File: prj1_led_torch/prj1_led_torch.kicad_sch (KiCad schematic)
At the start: 4 parts, among them SW1 SW_SPST

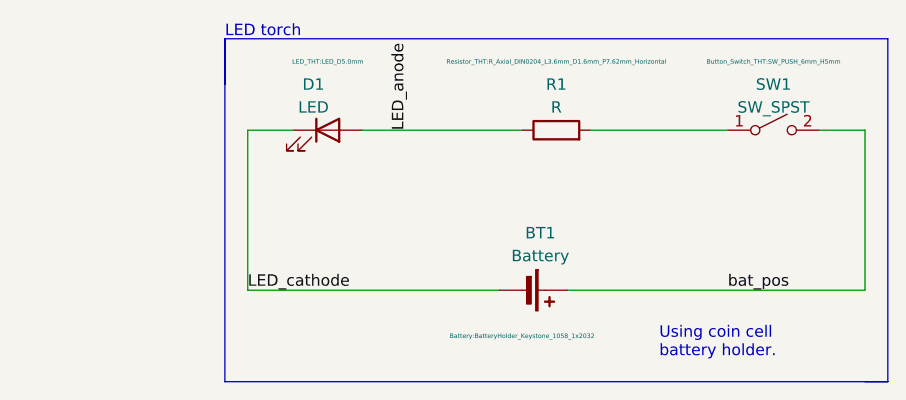
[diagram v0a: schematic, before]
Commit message: Creata simulazione circuitale
Feat: preparata la simulazione per transitorio
Feat: creato il modello per il diodo LED
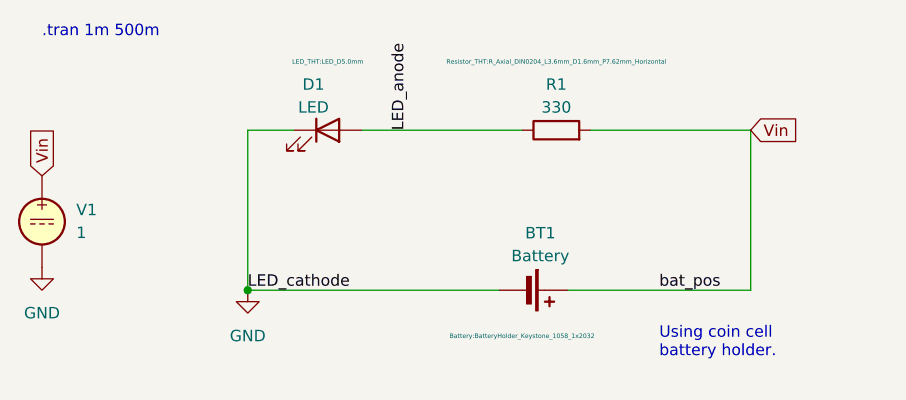
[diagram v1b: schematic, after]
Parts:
- removed SW1: SW_SPST, Button_Switch_THT:SW_PUSH_6mm_H5mm, symbol Switch:SW_SPST
- added V1: 1, symbol Simulation_SPICE:VDC
- R1: value R -> 330
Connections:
- net bat_pos is gone; now on net Vin: BT1.1 (+)
- net Vin: now reaches R1.2
- net Vin: now also V1.1
- net LED_cathode renamed GND
- net GND: now also V1.2
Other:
- note added: ".tran 1m 500m"
- note removed: "LED torch"
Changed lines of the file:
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@@
     (comment 2 "Filippo Graziani")
   )
+  (junction (at 116.84 109.22) (diameter 0) (color 0 0 0 0)
+  )
   (wire (pts (xy 129.54 91.44) (xy 147.32 91.44))
     (stroke (width 0) (type default))
   )
-  (polyline (pts (xy 114.3 81.28) (xy 114.3 86.36))
-    (stroke (width 0) (type default))
-  )
-  (wire (pts (xy 154.94 91.44) (xy 170.18 91.44))
-    (stroke (width 0) (type default))
-  )
-  (wire (pts (xy 185.42 91.44) (xy 185.42 109.22))
+  (wire (pts (xy 152.4 109.22) (xy 172.72 109.22))
+    (stroke (width 0) (type default))
+  )
+  (wire (pts (xy 172.72 91.44) (xy 172.72 109.22))
     (stroke (width 0) (type default))
   )
@@
     (stroke (width 0) (type default))
   )
-  (polyline (pts (xy 114.3 81.28) (xy 187.96 81.28))
-    (stroke (width 0) (type default))
-  )
-  (wire (pts (xy 152.4 109.22) (xy 185.42 109.22))
-    (stroke (width 0) (type default))
-  )
-  (polyline (pts (xy 187.96 119.38) (xy 114.3 119.38))
-    (stroke (width 0) (type default))
-  )
-  (polyline (pts (xy 114.3 81.28) (xy 114.3 119.38))
-    (stroke (width 0) (type default))
-  )
-  (wire (pts (xy 180.34 91.44) (xy 185.42 91.44))
-    (stroke (width 0) (type default))
-  )
-  (polyline (pts (xy 185.42 119.38) (xy 187.96 119.38))
-    (stroke (width 0) (type default))
-  )
-  (polyline (pts (xy 187.96 81.28) (xy 187.96 119.38))
+  (wire (pts (xy 154.94 91.44) (xy 172.72 91.44))
     (stroke (width 0) (type default))
   )
@@
     (effects (font (size 1.27 1.27)) (justify left bottom))
   )
-  (text "LED torch" (at 114.3 81.28 0)
+  (text ".tran 1m 500m" (at 93.98 81.28 0)
     (effects (font (size 1.27 1.27)) (justify left bottom))
   )
@@
     (effects (font (size 1.27 1.27)) (justify left bottom))
   )
-  (label "bat_pos" (at 170.18 109.22 0) (fields_autoplaced)
-    (effects (font (size 1.27 1.27)) (justify left bottom))
+  (label "bat_pos" (at 162.56 109.22 0) (fields_autoplaced)
+    (effects (font (size 1.27 1.27)) (justify left bottom))
+  )
+  (global_label "Vin" (shape input) (at 172.72 91.44 0) (fields_autoplaced)
+    (effects (font (size 1.27 1.27)) (justify left))
+    (property "Intersheetrefs" "${INTERSHEET_REFS}" (at 178.4682 91.44 0)
+      (effects (font (size 1.27 1.27)) (justify left) hide)
+    )
+  )
+  (global_label "Vin" (shape input) (at 93.98 96.52 90) (fields_autoplaced)
+    (effects (font (size 1.27 1.27)) (justify left))
+    (property "Intersheetrefs" "${INTERSHEET_REFS}" (at 93.98 90.7718 90)
+      (effects (font (size 1.27 1.27)) (justify left) hide)
+    )
+  )
+  (symbol (lib_id "power:GND") (at 93.98 106.68 0) (unit 1)
+    (in_bom yes) (on_board yes) (dnp no) (fields_autoplaced)
+    (property "Reference" "#PWR01" (at 93.98 113.03 0)
+      (effects (font (size 1.27 1.27)) hide)
+    )
+    (property "Value" "GND" (at 93.98 111.76 0)
+      (effects (font (size 1.27 1.27)))
+    )
+    (property "Footprint" "" (at 93.98 106.68 0)
+      (effects (font (size 1.27 1.27)) hide)
+    )
+    (property "Datasheet" "" (at 93.98 106.68 0)
+      (effects (font (size 1.27 1.27)) hide)
+    )
+    (pin "1")
+    (instances
+      (project "prj1_led_torch"
+        (path "/53546937-c78d-475c-81a9-f17052431549"
+          (reference "#PWR01") (unit 1)
+        )
+      )
+    )
   )
   (symbol (lib_id "Device:Battery_Cell") (at 147.32 109.22 270) (unit 1)
@@
       (effects (font (size 0.5 0.5)) hide)
     )
+    (property "Purpose" "" (at 147.32 109.22 0)
+      (effects (font (size 1.27 1.27)))
+    )
+    (property "Sim.Enable" "0" (at 147.32 109.22 0)
+      (effects (font (size 1.27 1.27)) hide)
+    )
     (pin "1")
     (pin "2")
@@
         (path "/53546937-c78d-475c-81a9-f17052431549"
           (reference "BT1") (unit 1)
+        )
+      )
+    )
+  )
+  (symbol (lib_id "Simulation_SPICE:VDC") (at 93.98 101.6 0) (unit 1)
+    (in_bom yes) (on_board yes) (dnp no) (fields_autoplaced)
+    (property "Reference" "V1" (at 97.79 100.2942 0)
+      (effects (font (size 1.27 1.27)) (justify left))
+    )
+    (property "Value" "1" (at 97.79 102.8342 0)
+      (effects (font (size 1.27 1.27)) (justify left))
+    )
+    (property "Footprint" "" (at 93.98 101.6 0)
+      (effects (font (size 1.27 1.27)) hide)
+    )
+    (property "Datasheet" "~" (at 93.98 101.6 0)
+      (effects (font (size 1.27 1.27)) hide)
+    )
+    (property "Sim.Pins" "1=+ 2=-" (at 93.98 101.6 0)
+      (effects (font (size 1.27 1.27)) hide)
+    )
+    (property "Sim.Type" "SIN" (at 93.98 101.6 0)
+      (effects (font (size 1.27 1.27)) hide)
+    )
+    (property "Sim.Device" "V" (at 93.98 101.6 0)
+      (effects (font (size 1.27 1.27)) (justify left) hide)
+    )
+    (property "Purpose" "" (at 93.98 101.6 0)
+      (effects (font (size 1.27 1.27)))
+    )
+    (property "Sim.Params" "dc=0 ampl=5 f=10" (at 93.98 101.6 0)
+      (effects (font (size 1.27 1.27)) hide)
+    )
+    (pin "1")
+    (pin "2")
+    (instances
+      (project "prj1_led_torch"
+        (path "/53546937-c78d-475c-81a9-f17052431549"
+          (reference "V1") (unit 1)
+        )
+      )
+    )
+  )
+  (symbol (lib_id "power:GND") (at 116.84 109.22 0) (unit 1)
+    (in_bom yes) (on_board yes) (dnp no) (fields_autoplaced)
+    (property "Reference" "#PWR02" (at 116.84 115.57 0)
+      (effects (font (size 1.27 1.27)) hide)
+    )
+    (property "Value" "GND" (at 116.84 114.3 0)
+      (effects (font (size 1.27 1.27)))
+    )
+    (property "Footprint" "" (at 116.84 109.22 0)
+      (effects (font (size 1.27 1.27)) hide)
+    )
+    (property "Datasheet" "" (at 116.84 109.22 0)
+      (effects (font (size 1.27 1.27)) hide)
+    )
+    (pin "1")
+    (instances
+      (project "prj1_led_torch"
+        (path "/53546937-c78d-475c-81a9-f17052431549"
+          (reference "#PWR02") (unit 1)
         )
       )
@@
       (effects (font (size 0.5 0.5)) hide)
     )
+    (property "Purpose" "" (at 125.73 91.44 0)
+      (effects (font (size 1.27 1.27)))
+    )
+    (property "Sim.Device" "D" (at 125.73 91.44 0)
+      (effects (font (size 1.27 1.27)) hide)
+    )
+    (property "Sim.Pins" "1=A 2=K" (at 125.73 91.44 0)
+      (effects (font (size 1.27 1.27)) hide)
+    )
+    (property "Sim.Library" "led2.model" (at 125.73 91.44 0)
+      (effects (font (size 1.27 1.27)) hide)
+    )
+    (property "Sim.Name" "LED2" (at 125.73 91.44 0)
+      (effects (font (size 1.27 1.27)) hide)
+    )
     (pin "1")
     (pin "2")
@@
         (path "/53546937-c78d-475c-81a9-f17052431549"
           (reference "D1") (unit 1)
-        )
-      )
-    )
-  )
-  (symbol (lib_id "Switch:SW_SPST") (at 175.26 91.44 0) (unit 1)
-    (in_bom yes) (on_board yes) (dnp no)
-    (property "Reference" "SW1" (at 175.26 86.36 0)
-      (effects (font (size 1.27 1.27)))
-    )
-    (property "Value" "SW_SPST" (at 175.26 88.9 0)
-      (effects (font (size 1.27 1.27)))
-    )
-    (property "Footprint" "Button_Switch_THT:SW_PUSH_6mm_H5mm" (at 175.26 83.82 0)
-      (effects (font (size 0.5 0.5)))
-    )
-    (property "Datasheet" "~" (at 175.26 91.44 0)
-      (effects (font (size 0.5 0.5)) hide)
-    )
-    (pin "1")
-    (pin "2")
-    (instances
-      (project "prj1_led_torch"
-        (path "/53546937-c78d-475c-81a9-f17052431549"
-          (reference "SW1") (unit 1)
         )
       )
@@
       (effects (font (size 1.27 1.27)))
     )
-    (property "Value" "R" (at 151.13 88.9 90)
+    (property "Value" "330" (at 151.13 88.9 90)
       (effects (font (size 1.27 1.27)))
     )
@@
       (effects (font (size 0.5 0.5)) hide)
     )
-    (pin "1")
+    (property "Purpose" "" (at 151.13 91.44 0)
+      (effects (font (size 1.27 1.27)))
+    )
+    (property "Sim.Device" "R" (at 151.13 91.44 0)
+      (effects (font (size 1.27 1.27)) hide)
+    )
+    (property "Sim.Pins" "1=+ 2=-" (at 151.13 91.44 0)
+      (effects (font (size 1.27 1.27)) hide)
+    )
+    (pin "1")
